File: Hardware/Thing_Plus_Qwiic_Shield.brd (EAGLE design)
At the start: 22.9 x 50.8 mm, 16 parts, among them J1 QWIIC_RIGHT_ANGLE, J2 QWIIC_RIGHT_ANGLE, J3 Vertical Qwiic Connector, J4 Vertical Qwiic Connector, U1 THING_PLUS

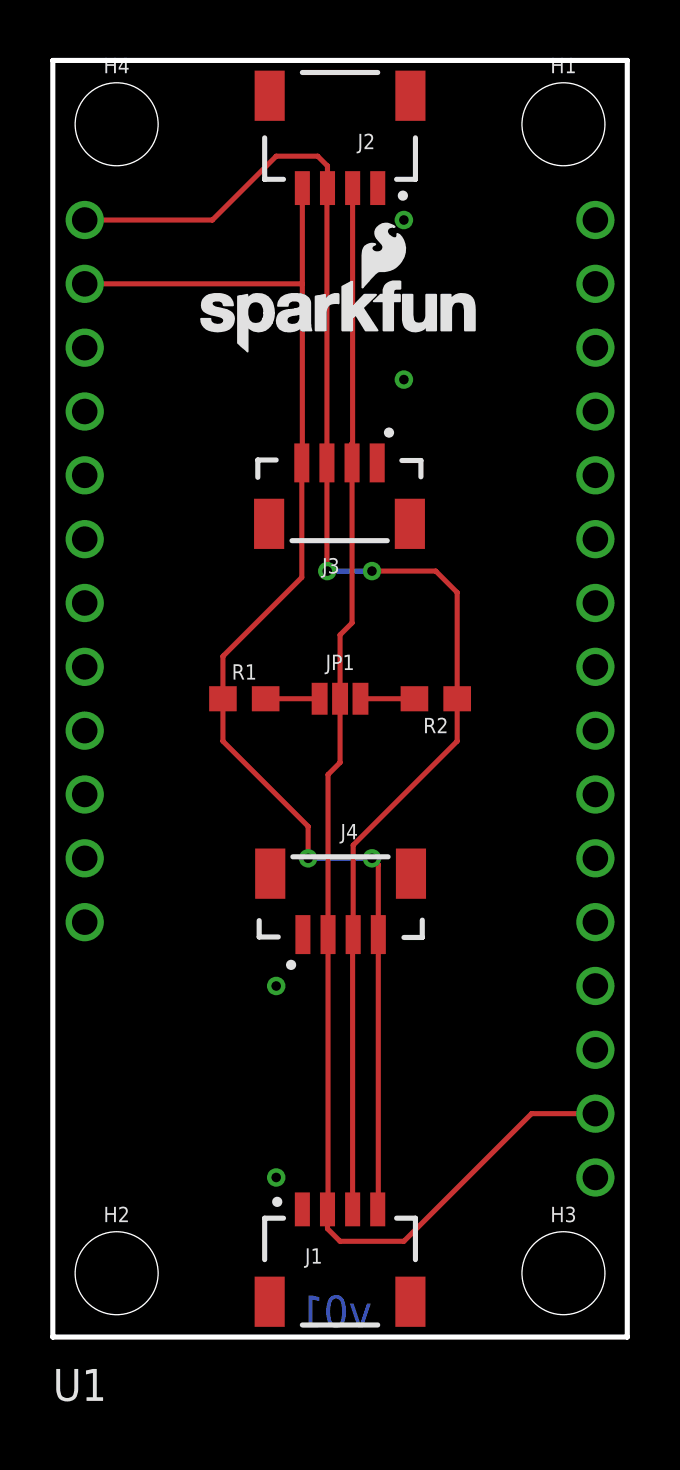
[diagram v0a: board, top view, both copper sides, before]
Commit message: panelizing and uploading gerbers
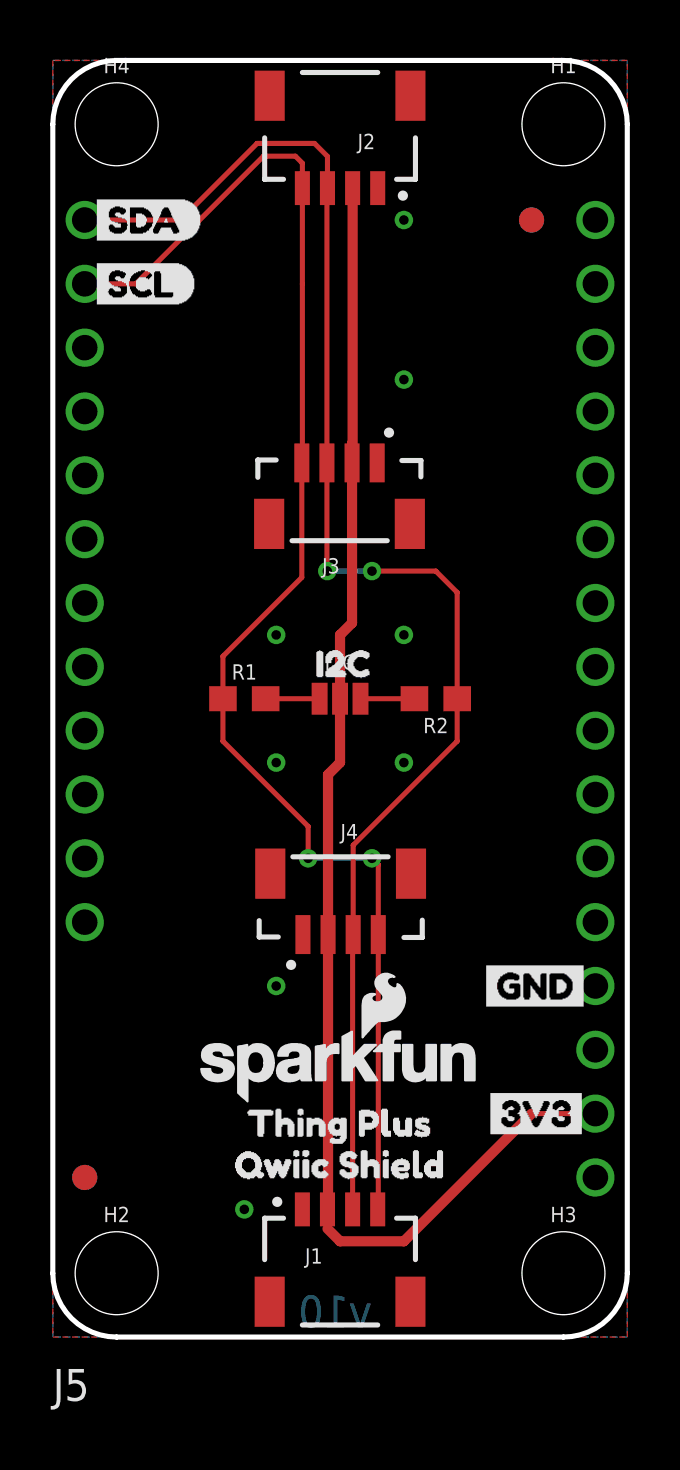
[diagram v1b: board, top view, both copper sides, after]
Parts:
- added FD1, FD2, FD3, FD4: FIDUCIAL1X2, SparkFun-Aesthetics:FIDUCIAL-1X2
- added U$1: (no value), buzzard_labels (25):THING_PLUS0
- added U$10: (no value), buzzard_labels (26):SCL3
- added U$11: (no value), buzzard_labels (26):SDA0
- added U$12: (no value), buzzard_labels (26):SDA2
- added U$2: (no value), buzzard_labels (25):_QWIIC_SHIELD1
- added U$3: (no value), buzzard_labels (24):3V36
- added U$4, U$5: (no value), buzzard_labels (23):3V36
- added U$6, U$7: (no value), buzzard_labels (23):GND0
- added U$8: (no value), buzzard_labels (23):I2C5
- added U$9: (no value), buzzard_labels (26):SCL1
- moved LOGO1 29.8 mm to (11.4, 10.8)
- moved FRAME1 2.84 mm to (-12.7, -12.7)
- renumbered JP1 to I2C, U1 to J5
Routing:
- net SCL: track 54.7 -> 57.9 mm
- net SDA: track 58.8 -> 59.4 mm
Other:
- outline, holes or cut-outs redrawn
- board text added: "A. England"
- board text added: "v10"
- board text removed: "v01"
